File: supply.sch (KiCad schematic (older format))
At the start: 59 parts, among them IC12 74HC00PW, IC13 SN74LVC1G126DCKR, IC4 TPS7A0518PDBVT, J12 533980471, T3 BSS138APW, U1 LM62440-Q1, U2 LM62440-Q1, U3 TXB0101DBVT

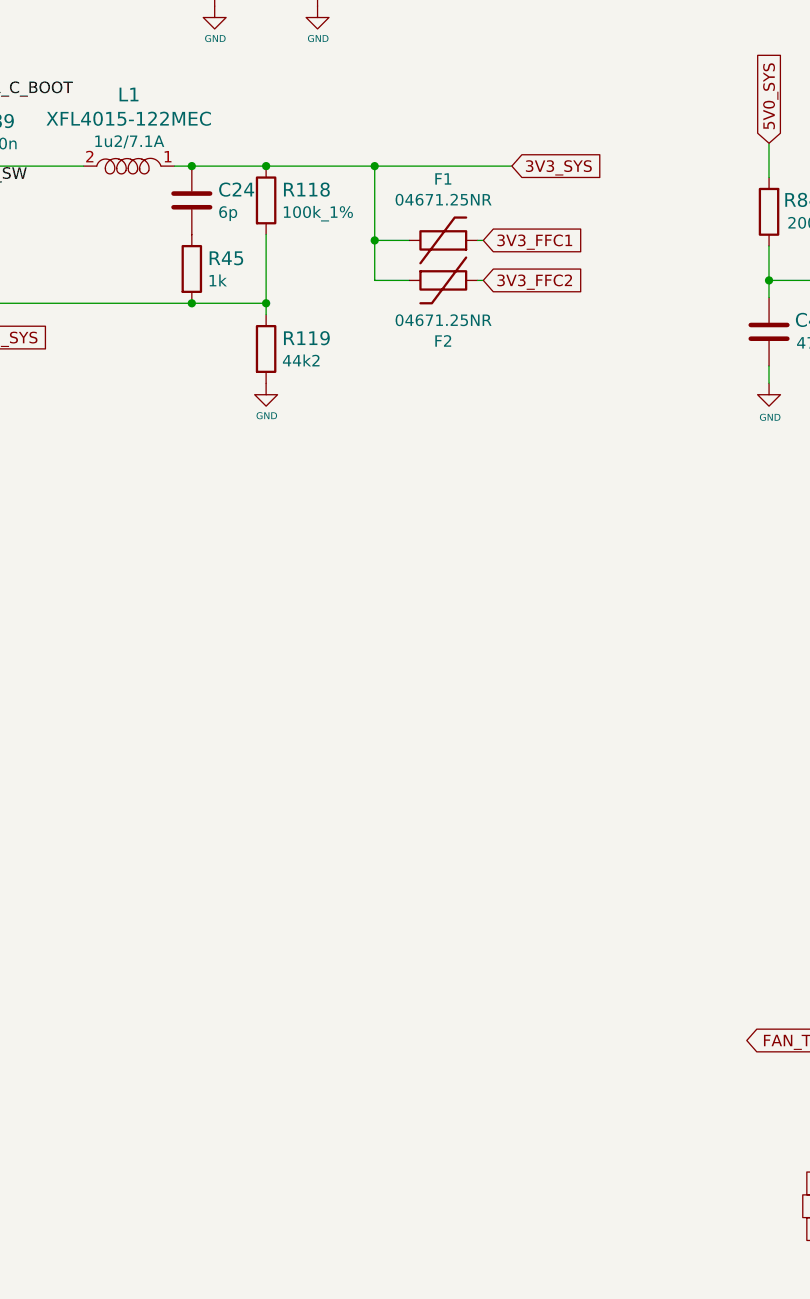
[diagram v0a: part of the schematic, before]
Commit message: Update 3V3 passives, add OR resistor to feedback network
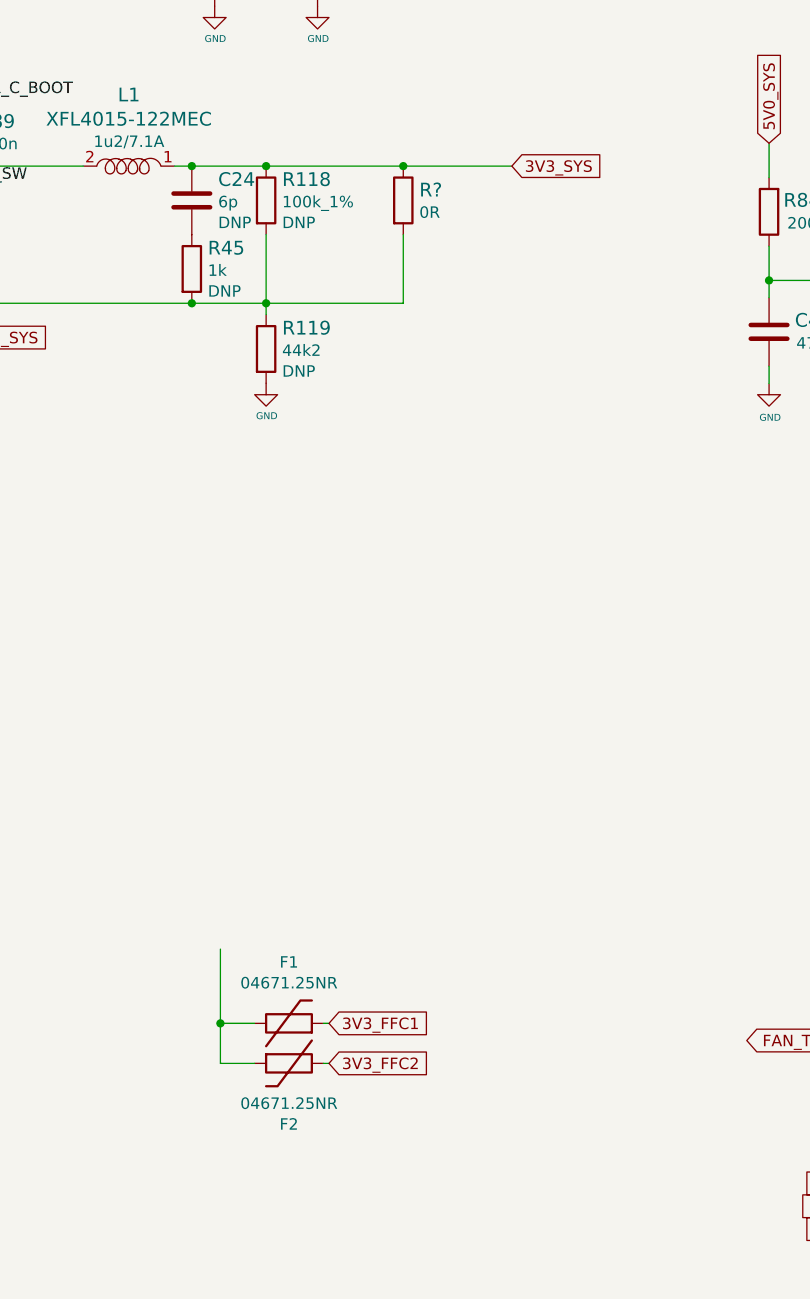
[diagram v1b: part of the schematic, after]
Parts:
- added R?: R_0R_0402, jetson-nano-baseboard-footprints:0402-res, symbol jetson-nano-baseboard:R_0R_0402
- C24, R118, R119, R45: DNP (none) -> DNP
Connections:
- wire segments 203 -> 205
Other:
- moved on the sheet: F1, F2
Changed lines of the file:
@@
 U 1 1 61E2F94A
 P 6275 5700
-F 0 "R118" V 6230 5770 60  0000 L CNN
+F 0 "R118" V 6184 5770 60  0000 L CNN
 F 1 "R_100k_1%_0402" H 6275 5550 60  0001 C CNN
 F 2 "jetson-nano-baseboard-footprints:0402" H 6475 5900 60  0001 L CNN
@@
 F 4 "PANASONIC" H 6475 6100 60  0001 L CNN "Manufacturer"
 F 5 "ERA-6AEB104V" H 6475 6000 60  0001 L CNN "MPN"
-F 6 "100k_1%" V 6328 5770 50  0000 L CNN "Val"
+F 6 "100k_1%" V 6282 5770 50  0000 L CNN "Val"
+F 7 "DNP" V 6373 5770 50  0000 L CNN "DNP"
 	1    6275 5700
 	0    1    1    0
@@
 Text GLabel 7350 5550 2    50   Input ~ 0
 3V3_SYS
-Wire Wire Line
-	6275 5550 6750 5550
-Wire Wire Line
-	6750 5550 7350 5550
 $Comp
 L jetson-nano-baseboard:R_44k2_0402 R119
 U 1 1 61FF4E81
 P 6275 6350
-F 0 "R119" V 6230 6420 60  0000 L CNN
+F 0 "R119" V 6184 6420 60  0000 L CNN
 F 1 "R_44k2_0402" H 6275 6200 60  0001 C CNN
 F 2 "jetson-nano-baseboard-footprints:0402-res" H 6475 6550 60  0001 L CNN
@@
 F 4 "PANASONIC_ELECTRONIC_COMPONENTS" H 6475 6750 60  0001 L CNN "Manufacturer"
 F 5 "ERJ2RKF4422X" H 6475 6650 60  0001 L CNN "MPN"
-F 6 "44k2" V 6328 6420 50  0000 L CNN "Val"
+F 6 "44k2" V 6282 6420 50  0000 L CNN "Val"
+F 7 "DNP" V 6373 6420 50  0000 L CNN "DNP"
 	1    6275 6350
 	0    1    1    0
 $EndComp
-Text GLabel 7225 5875 2    50   Input ~ 0
+Text GLabel 6550 9300 2    50   Input ~ 0
 3V3_FFC1
-Text GLabel 7225 6050 2    50   Input ~ 0
+Text GLabel 6550 9475 2    50   Input ~ 0
 3V3_FFC2
-Connection ~ 6750 5550
 Wire Wire Line
 	4900 5550 5475 5550
@@
 U 1 1 62A91D2C
 P 5950 6000
-F 0 "R45" V 5905 6070 60  0000 L CNN
+F 0 "R45" V 5859 6070 60  0000 L CNN
 F 1 "R_1k_0402" H 5950 5850 60  0001 C CNN
 F 2 "jetson-nano-baseboard-footprints:0402-res" H 6150 6200 60  0001 L CNN
@@
 F 4 "BOURNS" H 6150 6400 60  0001 L CNN "Manufacturer"
 F 5 "CR0402-FX-1001GLF" H 6150 6300 60  0001 L CNN "MPN"
-F 6 "1k" V 6003 6070 50  0000 L CNN "Val"
+F 6 "1k" V 5957 6070 50  0000 L CNN "Val"
+F 7 "DNP" V 6048 6070 50  0000 L CNN "DNP"
 	1    5950 6000
 	0    1    1    0
@@
 U 1 1 62A91D35
 P 5950 5700
-F 0 "C24" H 6065 5745 60  0000 L CNN
+F 0 "C24" H 6065 5791 60  0000 L CNN
 F 1 "C_6p_0402" H 5950 5550 60  0001 C CNN
 F 2 "jetson-nano-baseboard-footprints:0402-cap" H 6150 5900 60  0001 L CNN
@@
 F 4 "WALSIN" H 6150 6100 60  0001 L CNN "Manufacturer"
 F 5 "0402N6R0D500CT" H 6150 6000 60  0001 L CNN "MPN"
-F 6 "6p" H 6065 5647 50  0000 L CNN "Val"
+F 6 "6p" H 6065 5693 50  0000 L CNN "Val"
+F 7 "DNP" H 6065 5602 50  0000 L CNN "DNP"
 	1    5950 5700
 	1    0    0    -1
@@
 	4525 2475 4575 2475
 Wire Wire Line
-	7225 5875 7200 5875
-Wire Wire Line
-	7225 6050 7200 6050
-Wire Wire Line
-	6900 5875 6750 5875
-Connection ~ 6750 5875
-Wire Wire Line
-	6750 5875 6750 6050
-Wire Wire Line
-	6750 5550 6750 5875
+	6550 9300 6525 9300
+Wire Wire Line
+	6550 9475 6525 9475
+Wire Wire Line
+	6225 9300 6075 9300
+Connection ~ 6075 9300
+Wire Wire Line
+	6075 9300 6075 9475
+Wire Wire Line
+	6075 8975 6075 9300
 $Comp
 L jetson-nano-baseboard:04671.25NR F1
 U 1 1 618DBB7C
-P 7050 5875
-F 0 "F1" H 7050 6142 50  0000 C CNN
-F 1 "04671.25NR" H 7050 6051 50  0000 C CNN
-F 2 "jetson-nano-baseboard-footprints:0603-Fuse-Littelfuse-0467" H 7100 5650 50  0001 C CNN
-F 3 "https://www.littelfuse.com/~/media/electronics/datasheets/fuses/littelfuse_fuse_467_datasheet.pdf.pdf" H 7050 5725 50  0001 C CNN
-F 4 "04671.25NR" H 7075 5575 50  0001 C CNN "MPN"
-F 5 "Littelfuse Inc." H 7100 5500 50  0001 C CNN "Manufacturer"
-	1    7050 5875
+P 6375 9300
+F 0 "F1" H 6375 9567 50  0000 C CNN
+F 1 "04671.25NR" H 6375 9476 50  0000 C CNN
+F 2 "jetson-nano-baseboard-footprints:0603-Fuse-Littelfuse-0467" H 6425 9075 50  0001 C CNN
+F 3 "https://www.littelfuse.com/~/media/electronics/datasheets/fuses/littelfuse_fuse_467_datasheet.pdf.pdf" H 6375 9150 50  0001 C CNN
+F 4 "04671.25NR" H 6400 9000 50  0001 C CNN "MPN"
+F 5 "Littelfuse Inc." H 6425 8925 50  0001 C CNN "Manufacturer"
+	1    6375 9300
 	1    0    0    -1
 $EndComp
@@
 L jetson-nano-baseboard:04671.25NR F2
 U 1 1 618F00A3
-P 7050 6050
-F 0 "F2" H 7050 6317 50  0000 C CNN
-F 1 "04671.25NR" H 7050 6226 50  0000 C CNN
-F 2 "jetson-nano-baseboard-footprints:0603-Fuse-Littelfuse-0467" H 7100 5825 50  0001 C CNN
-F 3 "https://www.littelfuse.com/~/media/electronics/datasheets/fuses/littelfuse_fuse_467_datasheet.pdf.pdf" H 7050 5900 50  0001 C CNN
-F 4 "04671.25NR" H 7075 5750 50  0001 C CNN "MPN"
-F 5 "Littelfuse Inc." H 7100 5675 50  0001 C CNN "Manufacturer"
-	1    7050 6050
+P 6375 9475
+F 0 "F2" H 6375 9742 50  0000 C CNN
+F 1 "04671.25NR" H 6375 9651 50  0000 C CNN
+F 2 "jetson-nano-baseboard-footprints:0603-Fuse-Littelfuse-0467" H 6425 9250 50  0001 C CNN
+F 3 "https://www.littelfuse.com/~/media/electronics/datasheets/fuses/littelfuse_fuse_467_datasheet.pdf.pdf" H 6375 9325 50  0001 C CNN
+F 4 "04671.25NR" H 6400 9175 50  0001 C CNN "MPN"
+F 5 "Littelfuse Inc." H 6425 9100 50  0001 C CNN "Manufacturer"
+	1    6375 9475
 	-1   0    0    1
 $EndComp
@@
 $EndComp
 Wire Wire Line
-	6750 6050 6900 6050
+	6075 9475 6225 9475
 Connection ~ 2325 2100
 Wire Wire Line
@@
 	9425 9025 9425 9075
 Connection ~ 9225 9025
+Wire Wire Line
+	6275 5550 6875 5550
+$Comp
+L jetson-nano-baseboard:R_0R_0402 R?
+U 1 1 61DB825F
+P 6875 5700
+F 0 "R?" V 6830 5770 60  0000 L CNN
+F 1 "R_0R_0402" H 6875 5550 60  0001 C CNN
+F 2 "jetson-nano-baseboard-footprints:0402-res" H 7075 5900 60  0001 L CNN
+F 3 "" H 6875 5700 50  0001 C CNN
+F 4 "PANASONIC" H 7075 6100 60  0001 L CNN "Manufacturer"
+F 5 "ERJ2GE0R00X" H 7075 6000 60  0001 L CNN "MPN"
+F 6 "0R" V 6928 5770 50  0000 L CNN "Val"
+	1    6875 5700
+	0    1    1    0
+$EndComp
+Connection ~ 6875 5550
+Wire Wire Line
+	6875 5550 7350 5550
+Wire Wire Line
+	6875 5850 6875 6150
+Wire Wire Line
+	6875 6150 6275 6150
 $EndSCHEMATC

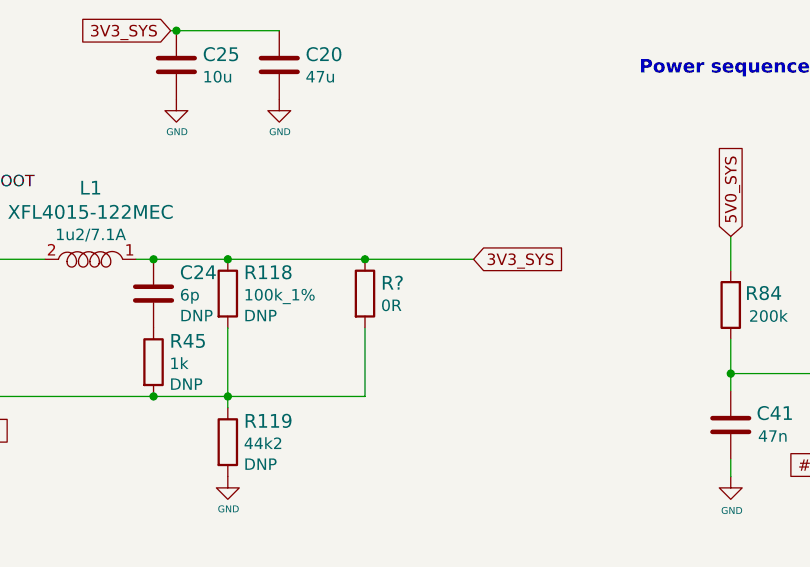
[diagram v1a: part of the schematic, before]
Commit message: Change IC15 to TPS7A0518, loclib
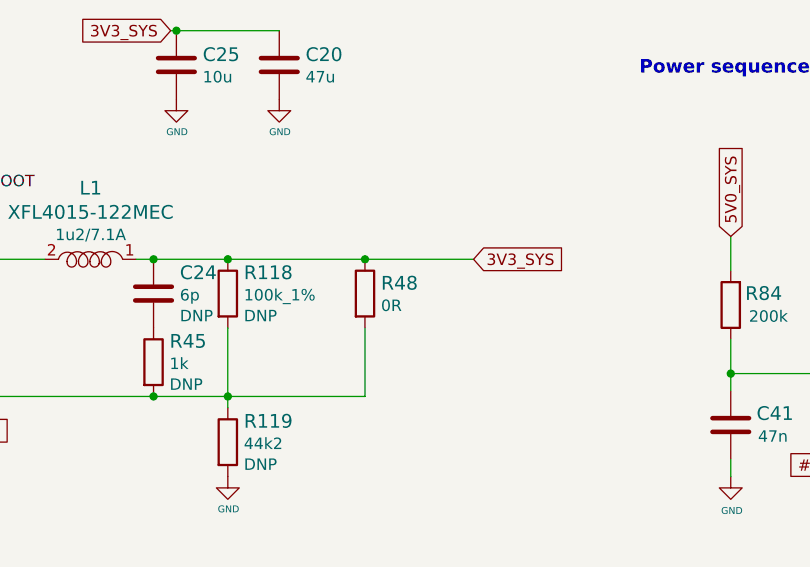
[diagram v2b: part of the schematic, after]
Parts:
- gave numbers to parts that had none: 1
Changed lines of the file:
@@
 	6275 5550 6875 5550
 $Comp
-L jetson-nano-baseboard:R_0R_0402 R?
+L jetson-nano-baseboard:R_0R_0402 R48
 U 1 1 61DB825F
 P 6875 5700
-F 0 "R?" V 6830 5770 60  0000 L CNN
+F 0 "R48" V 6830 5770 60  0000 L CNN
 F 1 "R_0R_0402" H 6875 5550 60  0001 C CNN
 F 2 "jetson-nano-baseboard-footprints:0402-res" H 7075 5900 60  0001 L CNN

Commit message: Change U3 to SN74LXC1T45DBVR
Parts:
- removed U3: TXB0101DBVT, jetson-nano-baseboard-footprints:SOT-23-6, symbol jetson-nano-baseboard:TXB0101DBVT
- added U3: SN74LXC1T45DBVR, jetson-nano-baseboard-footprints:SOT-23-6, symbol jetson-nano-baseboard:SN74LXC1T45DBVR
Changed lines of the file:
@@
 Wire Wire Line
 	1425 5250 2700 5250
-Text GLabel 9050 10100 0    50   Input ~ 0
-FAN_PWM
-Text GLabel 9025 10000 0    50   Input ~ 0
-1V8_SYS
-Wire Wire Line
-	9025 10000 9200 10000
-Wire Wire Line
-	9050 10100 9200 10100
-Text GLabel 9025 10200 0    50   Input ~ 0
-1V8_SYS
-Wire Wire Line
-	9025 10200 9200 10200
-Wire Wire Line
-	9800 10100 10300 10100
-Text Label 10300 10100 2    50   ~ 0
-FAN_PMW_5V
-Text GLabel 9925 9975 2    50   Input ~ 0
-5V0_SYS
-Wire Wire Line
-	9925 9975 9850 9975
-Wire Wire Line
-	9850 9975 9850 10000
-Wire Wire Line
-	9850 10000 9800 10000
-Wire Wire Line
-	9800 10200 9900 10200
-Wire Wire Line
-	9900 10200 9900 10300
-$Comp
-L jetson-nano-baseboard:GND #GND_0151
-U 1 1 61D0F309
-P 9900 10300
-F 0 "#GND_0151" H 9900 10300 20  0001 C CNN
-F 1 "GND" H 9903 10157 30  0000 C CNN
-F 2 "" H 9900 10300 70  0001 C CNN
-F 3 "" H 9900 10300 70  0001 C CNN
-	1    9900 10300
-	1    0    0    -1
-$EndComp
-$Comp
-L jetson-nano-baseboard:TXB0101DBVT U3
-U 1 1 62015C4C
-P 9500 10100
-F 0 "U3" H 9500 10447 60  0000 C CNN
-F 1 "TXB0101DBVT" H 9500 10341 60  0000 C CNN
-F 2 "jetson-nano-baseboard-footprints:SOT-23-6" H 9700 10300 60  0001 L CNN
-F 3 "https://www.ti.com/general/docs/suppproductinfo.tsp?distId=10&gotoUrl=https%3A%2F%2Fwww.ti.com%2Flit%2Fgpn%2Ftxb0101" H 9700 10400 60  0001 L CNN
-F 4 "TXB0101DBVT" H 9700 10500 60  0001 L CNN "MPN"
-F 5 "Texas Instruments" H 9700 10600 60  0001 L CNN "Manufacturer"
-	1    9500 10100
-	1    0    0    -1
-$EndComp
 Text Notes 11400 8975 0    59   ~ 12
 FAN 5V
@@
 Wire Wire Line
 	6875 6150 6275 6150
+Text GLabel 9050 10250 0    50   Input ~ 0
+FAN_PWM
+Text GLabel 9025 10150 0    50   Input ~ 0
+1V8_SYS
+Wire Wire Line
+	9025 10150 9200 10150
+Wire Wire Line
+	9050 10250 9200 10250
+Text GLabel 9025 10350 0    50   Input ~ 0
+1V8_SYS
+Wire Wire Line
+	9025 10350 9200 10350
+Wire Wire Line
+	9800 10250 10300 10250
+Text Label 10300 10250 2    50   ~ 0
+FAN_PMW_5V
+Text GLabel 9925 10125 2    50   Input ~ 0
+5V0_SYS
+Wire Wire Line
+	9925 10125 9850 10125
+Wire Wire Line
+	9850 10125 9850 10150
+Wire Wire Line
+	9850 10150 9800 10150
+Wire Wire Line
+	9800 10350 9900 10350
+Wire Wire Line
+	9900 10350 9900 10450
+$Comp
+L jetson-nano-baseboard:GND #GND_0151
+U 1 1 61D0F309
+P 9900 10450
+F 0 "#GND_0151" H 9900 10450 20  0001 C CNN
+F 1 "GND" H 9903 10307 30  0000 C CNN
+F 2 "" H 9900 10450 70  0001 C CNN
+F 3 "" H 9900 10450 70  0001 C CNN
+	1    9900 10450
+	1    0    0    -1
+$EndComp
+$Comp
+L jetson-nano-baseboard:SN74LXC1T45DBVR U3
+U 1 1 61E748D7
+P 9500 10250
+F 0 "U3" H 9500 10597 60  0000 C CNN
+F 1 "SN74LXC1T45DBVR" H 9500 10491 60  0000 C CNN
+F 2 "jetson-nano-baseboard-footprints:SOT-23-6" H 9700 10450 60  0001 L CNN
+F 3 "https://www.ti.com/lit/ds/symlink/sn74lxc1t45.pdf?ts=1641200283005&ref_url=https%253A%252F%252Fwww.ti.com%252Fstore%252Fti%252Fen%252Fp%252Fproduct%252F%253Fp%253DSN74LXC1T45DBVR%2526keyMatch%253DSN74LXC1T45DBVR%2526tisearch%253Dsearch-everything%2526usecase%253DOPN" H 9700 10550 60  0001 L CNN
+F 4 "SN74LXC1T45DBVR" H 9700 10650 60  0001 L CNN "MPN"
+F 5 "Texas Instruments" H 9700 10750 60  0001 L CNN "Manufacturer"
+	1    9500 10250
+	1    0    0    -1
+$EndComp
 $EndSCHEMATC

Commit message: Loclib, update schematic 5Vof  DCDC and 3V3DCDC for cameras
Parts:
- removed C16, C18: C_10u_1206_50V, jetson-nano-baseboard-footprints:1206-cap, symbol jetson-nano-baseboard:C_10u_1206_50V
- removed C17: C_47u_0805, jetson-nano-baseboard-footprints:0805-cap, symbol jetson-nano-baseboard:C_47u_0805
- removed C22: C_6p_0402, jetson-nano-baseboard-footprints:0402-cap, symbol jetson-nano-baseboard:C_6p_0402
- removed C23: C_10u_0805, jetson-nano-baseboard-footprints:0805-cap, symbol jetson-nano-baseboard:C_10u_0805
- removed C88: C_1u_0402, jetson-nano-baseboard-footprints:0402-cap, symbol jetson-nano-baseboard:C_1u_0402
- removed C90: C_100n_0402, jetson-nano-baseboard-footprints:0402-cap, symbol jetson-nano-baseboard:C_100n_0402
- removed FB4: 742792022, jetson-nano-baseboard-footprints:0805-cap, symbol jetson-nano-baseboard:Ferrite_Bead_Small
- removed L4: XEL4030-222MEC, jetson-nano-baseboard-footprints:Coilcraft-XEL4030, symbol jetson-nano-baseboard:XEL4030-222MEC
- removed R117: R_100k_0402, jetson-nano-baseboard-footprints:0402-res, symbol jetson-nano-baseboard:R_100k_0402
- removed R120: R_100k_1%_0402, jetson-nano-baseboard-footprints:0402, symbol jetson-nano-baseboard:R_100k_1%_0402
- removed R121: R_24k9_0.1%_0402, jetson-nano-baseboard-footprints:0402-res, symbol jetson-nano-baseboard:R_24k9_0.1%_0402
- removed R39: R_1k_0402, jetson-nano-baseboard-footprints:0402-res, symbol jetson-nano-baseboard:R_1k_0402
- removed U1: LM62440-Q1, jetson-nano-baseboard-footprints:VQFN-14-HR, symbol jetson-nano-baseboard:LM62440-Q1
- added C16, C18: C_2u2_0402, jetson-nano-baseboard-footprints:0402-cap, symbol jetson-nano-baseboard:C_2u2_0402
- added C17, C22: C_10u_1206_50V, jetson-nano-baseboard-footprints:1206-cap, symbol jetson-nano-baseboard:C_10u_1206_50V
- added C23, C55, C81: C_10u_0603, jetson-nano-baseboard-footprints:0603-cap, symbol jetson-nano-baseboard:C_10u_0603
- added C28: C_270p_25V_0402, jetson-nano-baseboard-footprints:0402-res, symbol jetson-nano-baseboard:C_270p_25V_0402
- added C56: C_100n_0402_50V, jetson-nano-baseboard-footprints:0402-cap, symbol jetson-nano-baseboard:C_100n_0402_50V
- added C57, C83: C_100n_0402, jetson-nano-baseboard-footprints:0402-cap, symbol jetson-nano-baseboard:C_100n_0402
- added C58: C_33n_0402, jetson-nano-baseboard-footprints:0402-cap, symbol jetson-nano-baseboard:C_33n_0402
- added C59, C64: C_47u_0805, jetson-nano-baseboard-footprints:0805-cap, symbol jetson-nano-baseboard:C_47u_0805
- added C61, C82: C_1n2_50V_0402, jetson-nano-baseboard-footprints:0402-res, symbol jetson-nano-baseboard:C_1n2_50V_0402
- added C84: C_1u_0402, jetson-nano-baseboard-footprints:0402-cap, symbol jetson-nano-baseboard:C_1u_0402
- added C85: C_4u7_0603, jetson-nano-baseboard-footprints:0603-cap, symbol jetson-nano-baseboard:C_4u7_0603
- added FB1: 74279221100, jetson-nano-baseboard-footprints:1206-res, symbol jetson-nano-baseboard:74279221100
- added L4: IHLP3232DZER3R3M01, jetson-nano-baseboard-footprints:IHLP3232DZ, symbol jetson-nano-baseboard:IHLP3232DZER3R3M01
- added L5, L6: LQH32PN2R2NN0L, jetson-nano-baseboard-footprints:LQH32PN2R2NN0L, symbol jetson-nano-baseboard:LQH32PN2R2NN0L
- added R117: R_52k3_0402, jetson-nano-baseboard-footprints:0402-res, symbol jetson-nano-baseboard:R_52k3_0402
- added R120, R39, R52: R_10k_0402, jetson-nano-baseboard-footprints:0402-res, symbol jetson-nano-baseboard:R_10k_0402
- added R74: R_2k_0402, jetson-nano-baseboard-footprints:0402-res, symbol jetson-nano-baseboard:R_2k_0402
- added R75: R_316k_0402, jetson-nano-baseboard-footprints:0402-res, symbol jetson-nano-baseboard:R_316k_0402
- added R76, R93: R_0R_0402, antmicro-footprints:0402-res, symbol antmicroResistors0402:R_0R_0402
- added R77: R_60k4_1%_0402, jetson-nano-baseboard-footprints:0402-res, symbol jetson-nano-baseboard:R_60k4_1%_0402
- added R89: R_3R3_0402, jetson-nano-baseboard-footprints:0402-res, symbol jetson-nano-baseboard:R_3R3_0402
- added R90: R_26k7_0402, jetson-nano-baseboard-footprints:0402-res, symbol jetson-nano-baseboard:R_26k7_0402
- added R91, R96: R_100k_0402, jetson-nano-baseboard-footprints:0402-res, symbol jetson-nano-baseboard:R_100k_0402
- added R94: R_8k66_1%_0402, jetson-nano-baseboard-footprints:0402-res, symbol jetson-nano-baseboard:R_8k66_1%_0402
- added TP11, TP12, TP15, TP41: Testpad, jetson-nano-baseboard-footprints:TP-R-1.5, symbol jetson-nano-baseboard:Testpad
- added TP5, TP8: ~, jetson-nano-baseboard-footprints:TP-R-1.5, symbol jetson-nano-baseboard:Testpad
- added U1, U5: LM3671MF-1.5_NOPB, jetson-nano-baseboard-footprints:SOT-23-5, symbol jetson-nano-baseboard:LM3671MF-1.5_NOPB
- added U6: SIC477ED-T1-GE3, antmicro-footprints:SIC47XED-T1-GE3, symbol antmicroDCDCConverters:SIC477ED-T1-GE3
- TP40: value ~ -> Testpad
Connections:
- net #RESET: now also R39.2, R52.2
- net 5V0_SYS: now also C16.1, C18.1, C59.1, C64.1, C81.1, C82.1, C83.2, L4.2 (P), R117.1, R93.1, TP41.1 (P), U1.1 (Vin), U5.1 (Vin)
- net 5V_FB: now also R117.2, R120.1, U6.22 (VFB)
- net 5V_SW: now also L4.1 (P), R94.1, U6.12 (SW), U6.13 (SW), U6.14 (SW)
- net 5V_VIN: now also C17.1, C22.1, C56.1, FB1.2, R91.2, TP11.1 (P), U6.1 (VCIN), U6.7 (VIN), U6.8 (VIN)
- net GND: now also C16.2, C17.2, C18.2, C22.2, C23.2, C28.1, C55.2, C56.2, C58.2, C59.2, C64.2, C81.2, C83.1, C84.2, C85.2, R120.2, R74.2, R77.2, R90.2, TP12.1 (P), U1.2 (GND), U5.2 (GND), U6.10 (PGND), U6.11 (PGND), U6.17 (PGND), U6.23 (AGND), U6.28 (AGND), U6.9 (PGND)
- net PWR_GOOD: now also R96.2, U6.2 (PGOOD)
- net VIN: now also FB1.1
- net at F1.1: now also C23.1, L5.2 (P), TP5.1 (P), U1.4 (FB); no longer F2.2
- new net: C55.1, F2.2, L6.2 (P), TP8.1 (P), U5.4 (FB)
- new net: C57.2, R89.1
- new net: R39.1, U1.3 (EN)
- new net: L5.1 (P), U1.5 (SW)
- new net: R52.1, U5.3 (EN)
- new net: L6.1 (P), U5.5 (SW)
- new net: C61.2, R93.2, U6.20 (VOUT)
- new net: C28.2, R75.2
- new net 5V_BOOT: C57.1, U6.4 (BOOT)
- new net 5V_COMP: R75.1, U6.21 (NC)
- new net 5V_EN: R91.1, TP15.1 (P), U6.3 (EN)
- new net 5V_FSW: R90.1, U6.24 (FSW)
- new net 5V_ILIM: R76.1, R77.1, U6.25 (ILIMIT)
- new net 5V_MODE: R74.1, U6.27 (MODE)
- new net 5V_PHASE: R89.2, U6.5 (PHASE), U6.6 (PHASE)
- new net 5V_SNS: C61.1, C82.2, R94.2
- new net 5V_SS: C58.1, U6.19 (SS)
- new net VDD_5V_DCDC: C84.1, R76.2, R96.1, U6.26 (VDD)
- new net VDRV_5V_DCDC: C85.1, U6.16 (VDRV)
- no-connect marks 1 -> 3
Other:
- note added: "0.8V typ"
- note added: "12A"
- note added: "1MHz"
- note added: "3V3 FFC 1&2"
- note added: "52k3 -> 4.98V"
- note added: "52k5 -> 5.0V"
- note added: "5V/8A"
- note added: "Note:\nPlace close \nto the feedback \nresistors"
- note added: "Note:\nSIC477 can be substituted with SIC472.\nIf so:\nR43, R41, R58, C24, C32, C39 are populated,\nR74, R75 are DNP"
- note added: "Power save mode enabled, \nVDD, VDRVPre-reg on"
- note added: "R_FB_H = R_FB_L * (V_OUT - V_FB) / V_FB \n10k * (5 - 0.8) / 0.8 = 52K5"
- note removed: "5V/4A"
- moved on the sheet: C19, C20, C21, C24, C25, C60, C65, C87, C89, F1, F2, FB3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
